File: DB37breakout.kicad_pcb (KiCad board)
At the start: 2 copper layers, 482.6 x 44.5 mm, 34 parts, among them J10 Conn_Coaxial, J11 Conn_Coaxial, J12 Conn_Coaxial, J13 Conn_Coaxial, J14 Conn_Coaxial, J15 Conn_Coaxial, J16 Conn_Coaxial, J17 Conn_Coaxial, J18 Conn_Coaxial, J19 Conn_Coaxial, J2 Conn_Coaxial, J20 Conn_Coaxial, J21 Conn_Coaxial, J22 Conn_Coaxial, J23 Conn_Coaxial, J24 Conn_Coaxial, J25 Conn_Coaxial, J26 Conn_Coaxial, J27 Conn_Coaxial, J28 Conn_Coaxial, J29 Conn_Coaxial, J3 Conn_Coaxial, J30 Conn_Coaxial, J31 Conn_Coaxial, J32 Conn_Coaxial, J33 Conn_Coaxial, J4 Conn_Coaxial, J5 Conn_Coaxial, J6 Conn_Coaxial, J7 Conn_Coaxial, J8 Conn_Coaxial, J9 Conn_Coaxial

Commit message: Adjusted paper size inn schematic and PCB editors
Adjusted paper size inn schematic and PCB editors
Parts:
- moved J11 244.5 mm to (72.9, 245.7)
- moved J12 244.5 mm to (73.6, 223.5)
- moved J14 244.5 mm to (127.6, 223.5)
- moved J15 244.5 mm to (154.5, 223.5)
- moved J18 244.5 mm to (235.4, 223.5)
- moved J20 244.5 mm to (289.4, 223.5)
- moved J21 244.5 mm to (316.4, 223.5)
- moved J22 244.5 mm to (343.3, 223.5)
- moved J23 244.5 mm to (370.3, 223.5)
- moved J26 244.5 mm to (451.2, 223.5)
- moved J28 244.5 mm to (505.2, 223.5)
- moved J29 244.5 mm to (532.1, 223.5)
- moved J30 244.5 mm to (532.3, 245.3)
- moved J31 244.5 mm to (511.4, 245.3)
- moved J32 244.5 mm to (490.6, 245.3)
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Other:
- board size 482.6 x 44.5 mm -> 482.6 x 44.4 mm

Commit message: Changed BNC footprint to vertical Through Hole; redesigned board with greater space between traces and footprints; shortened board length and expanded board width to lightly less than a 2U space
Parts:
- added H1: MountingHole, MountingHole:MountingHole_3mm, F.Cu at (211.9, 183.2)
- added H2: MountingHole, MountingHole:MountingHole_3mm, F.Cu at (211.2, 242.8)
- added H3: MountingHole, MountingHole:MountingHole_3mm, F.Cu at (361.8, 183.2)
- added H4: MountingHole, MountingHole:MountingHole_3mm, F.Cu at (361.8, 242.8)
- added H5: MountingHole, MountingHole:MountingHole_3mm, F.Cu at (511.7, 183.2)
- added H6: MountingHole, MountingHole:MountingHole_3mm, F.Cu at (512.4, 242.8)
- added REF**: BNC_TEConnectivity_1478204_Vertical, Connector_Coaxial:BNC_TEConnectivity_1478204_Vertical, F.Cu at (79.9, -119.1)
- J10, J11, J12, J13, J14, J15, J16, J17, J18, J19, J2, J20, J21, J22, J23, J24, J25, J26, J27, J28, J29, J3, J30, J31, J32, J33, J4, J5, J6, J7, J8, J9: footprint Connector_Coaxial:BNC_Amphenol_031-5539_Vertical -> Connector_Coaxial:BNC_TEConnectivity_1478204_Vertical
- moved J11 224.4 mm to (293.0, 201.9)
- moved J12 223.3 mm to (293.0, 181.8)
- moved J13 221.0 mm to (320.5, 201.9)
- moved J10 199.7 mm to (293.0, 229.1)
- moved J14 197.4 mm to (320.5, 181.8)
- moved J16 168.0 mm to (348.1, 201.9)
- moved J15 166.1 mm to (320.5, 229.1)
- moved J9 151.4 mm to (265.5, 229.1)
- moved J8 144.4 mm to (265.5, 181.8)
- moved J17 139.7 mm to (348.1, 229.1)
- moved J19 139.5 mm to (401.8, 229.1)
- moved J18 138.9 mm to (374.3, 229.1)
- moved J7 116.9 mm to (265.5, 201.9)
- moved J21 88.1 mm to (401.8, 201.9)
- moved J20 87.6 mm to (374.3, 201.9)
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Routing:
- net /AIN9+: track 226.8 -> 33.6 mm
- net /AIN10+: track 251.3 -> 60.4 mm
- net /AIN12+: track 236.6 -> 54.5 mm
- net /AIN11+: track 260.9 -> 81.7 mm
- net /AIN9-: track 226.4 -> 49.2 mm
- net /AIN10-: track 251.8 -> 77.2 mm
- net /AIN12-: track 232.5 -> 61.8 mm
- net /AIN14+: track 188.2 -> 26.4 mm
- net /AIN11-: track 256.7 -> 98.5 mm
- net /AIN8+: track 195.9 -> 53.6 mm
- net /AIN14-: track 184.1 -> 43.2 mm
- net /AIN13+: track 212.4 -> 72.6 mm
- net /AIN17+: track 174.5 -> 35.4 mm
- net /AIN8-: track 194.6 -> 63.0 mm
- net /AIN18+: track 150.8 -> 20.6 mm
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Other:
- board size 482.6 x 44.4 mm -> 326.2 x 87.7 mm
- board text added: "1Ux17in Space"
- board text added: "1Ux19in Space"
- board text added: "2Ux19in Space"
- board text added: "Board Outline"
- board text removed: "1U Space"

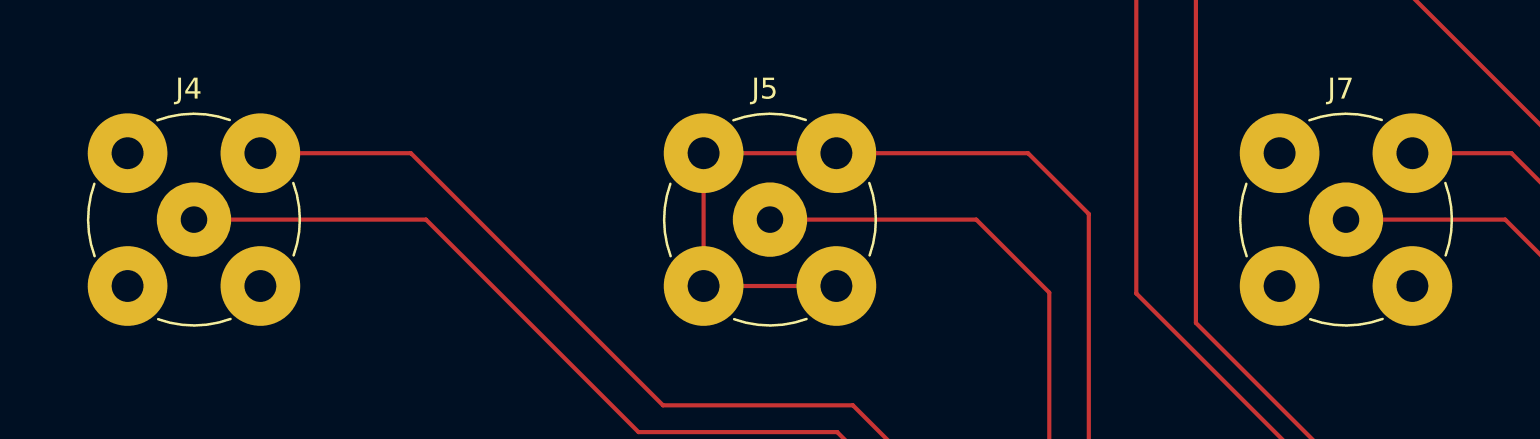
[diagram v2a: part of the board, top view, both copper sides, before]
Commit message: connected unconnected traces
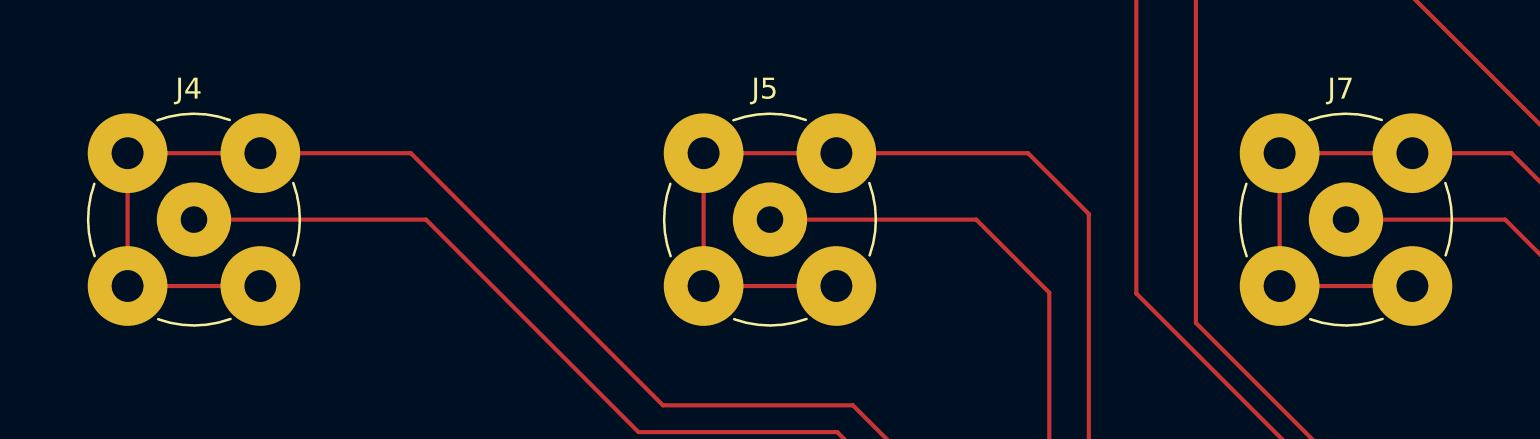
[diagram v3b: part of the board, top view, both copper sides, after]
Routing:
- net /AIN3-: track 105.8 -> 124.9 mm
- net /AIN6-: track 64.3 -> 83.4 mm
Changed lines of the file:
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@@
+	)
+	(segment
+		(start 213.560455 205.065)
+		(end 207.210455 205.065)
+		(width 0.2)
+		(layer "F.Cu")
+		(net 6)
 	)
 	(segment
@@
 	)
 	(segment
+		(start 213.560455 198.715)
+		(end 207.210455 198.715)
+		(width 0.2)
+		(layer "F.Cu")
+		(net 6)
+	)
+	(segment
 		(start 241.89 210.77)
 		(end 232.81 210.77)
@@
 	)
 	(segment
+		(start 207.210455 205.065)
+		(end 207.210455 198.715)
+		(width 0.2)
+		(layer "F.Cu")
+		(net 6)
+	)
+	(segment
 		(start 232.81 210.77)
 		(end 220.755 198.715)
@@
 	)
 	(segment
+		(start 268.642273 198.715)
+		(end 262.292273 198.715)
+		(width 0.2)
+		(layer "F.Cu")
+		(net 24)
+	)
+	(segment
 		(start 301.066471 246.835)
 		(end 285.49 231.258529)
@@
 	)
 	(segment
+		(start 268.642273 205.065)
+		(end 262.292273 205.065)
+		(width 0.2)
+		(layer "F.Cu")
+		(net 24)
+	)
+	(segment
 		(start 285.49 231.258529)
 		(end 285.49 210.83)
 		(width 0.2)
 		(layer "F.Cu")
+		(net 24)
+	)
+	(segment
+		(start 262.292273 205.065)
+		(end 262.292273 198.715)
+		(width 0.2)
+		(layer "F.Cu")
